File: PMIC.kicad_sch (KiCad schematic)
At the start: 57 parts, among them J10 Conn_01x03_Pin, J9 Conn_01x03_Pin, Q2 QM6015D, U7 MP2759AGQ-0000-Z, U8 MPM3620AGQV-P, U9 MPM3620AGQV-P

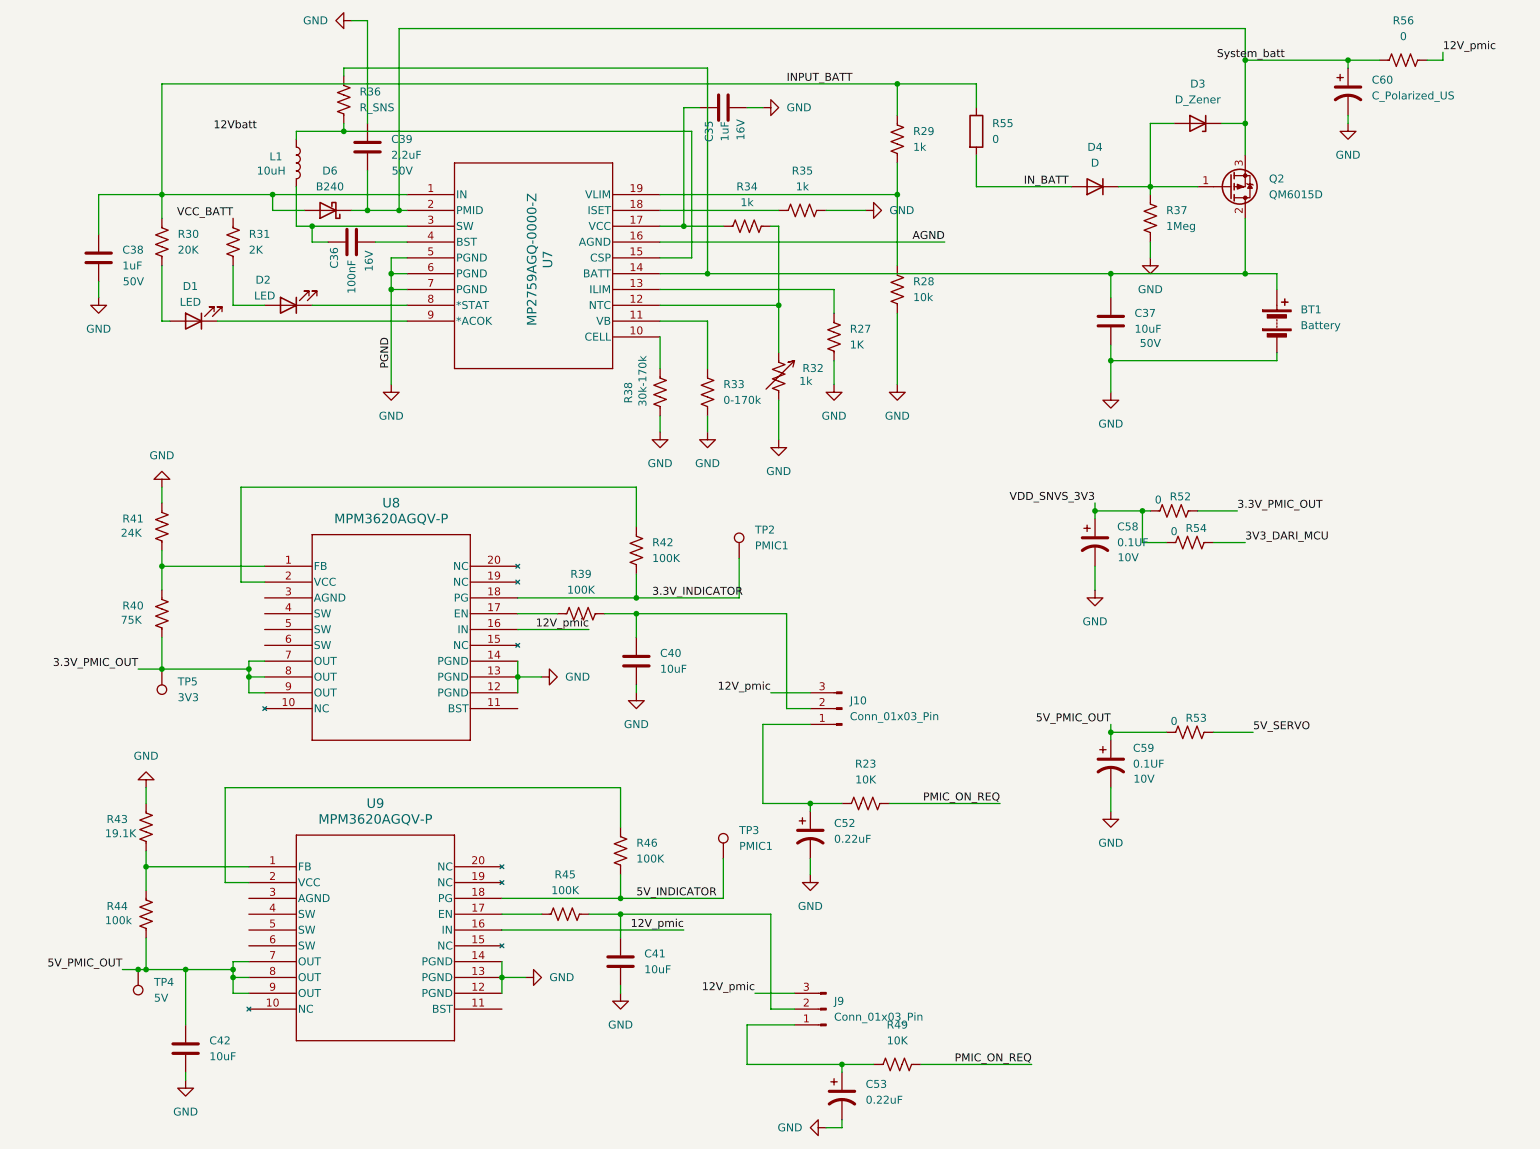
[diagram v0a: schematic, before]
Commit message: menambah lebih dari setengah footprint
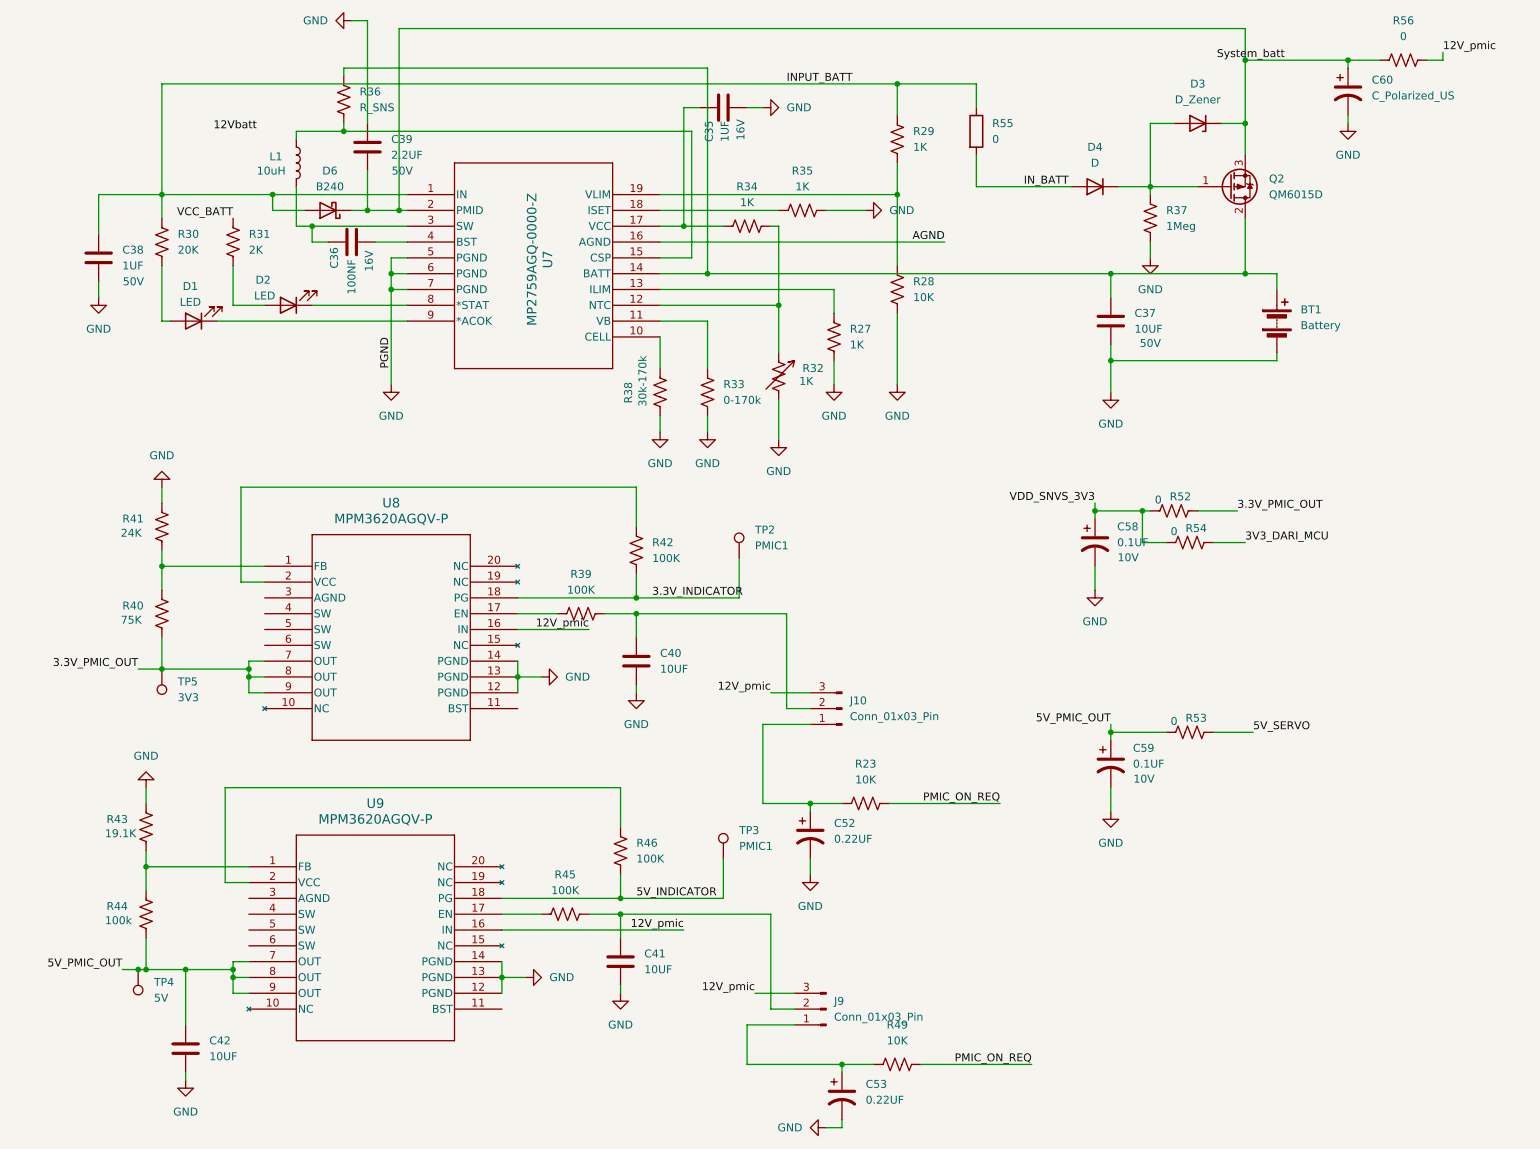
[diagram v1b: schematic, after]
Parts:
- C35, C38: value 1uF -> 1UF; footprint (none) -> Capacitor_SMD:C_0402_1005Metric
- C36: value 100nF -> 100NF; footprint (none) -> Capacitor_SMD:C_0402_1005Metric
- C37, C40, C41, C42: value 10uF -> 10UF; footprint (none) -> Capacitor_SMD:C_0603_1608Metric; MANUFACTURER (none) -> GRM188R61A106KE69D
- C39: value 2,2uF -> 2.2UF; footprint (none) -> Capacitor_SMD:C_0402_1005Metric
- C52, C53: value 0.22uF -> 0.22UF; footprint (none) -> Capacitor_SMD:C_0402_1005Metric; MANUFACTURER (none) -> CL10A226MQ8NRNE
- C58, C59: footprint (none) -> Capacitor_SMD:C_0402_1005Metric; MANUFACTURER (none) -> CC0402KRX5R6BB104
- R23, R27, R37, R39, R42, R44, R45, R46, R49, R52, R53, R54, R55, R56: footprint (none) -> Resistor_SMD:R_0402_1005Metric
- R28: value 10k -> 10K; footprint (none) -> Resistor_SMD:R_0402_1005Metric
- R29, R32, R34, R35: value 1k -> 1K; footprint (none) -> Resistor_SMD:R_0402_1005Metric
- U7: footprint QFN-19_MP2759A_MNP -> footprints:QFN-19_MP2759A_MNP
- U8, U9: footprint QFN3p0x5p0x1p6_MPM3606A_MNP -> footprints:QFN3p0x5p0x1p6_MPM3606A_MNP

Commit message: menambahkan beberapa component lagi
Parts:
- TP2, TP3, TP4, TP5: footprint (none) -> MountingHole:MountingHole_2.1mm
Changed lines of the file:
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@@
 			)
 		)
-		(property "Footprint" ""
+		(property "Footprint" "MountingHole:MountingHole_2.1mm"
 			(at 27.94 120.65 0)
 			(effects
@@
 			)
 		)
-		(property "Footprint" ""
+		(property "Footprint" "MountingHole:MountingHole_2.1mm"
 			(at 128.27 151.13 0)
 			(effects
@@
 			)
 		)
-		(property "Footprint" ""
+		(property "Footprint" "MountingHole:MountingHole_2.1mm"
 			(at 130.81 102.87 0)
 			(effects
@@
 			)
 		)
-		(property "Footprint" ""
+		(property "Footprint" "MountingHole:MountingHole_2.1mm"
 			(at 24.13 168.91 0)
 			(effects

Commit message: change the power bat system
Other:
- moved on the sheet: TP4
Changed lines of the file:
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@@
 	)
 	(junction
-		(at 29.21 168.91)
-		(diameter 0)
-		(color 0 0 0 0)
-	)
-	(junction
 		(at 207.01 33.02)
 		(diameter 0)
@@
 	)
 	(junction
+		(at 25.4 168.91)
+		(diameter 0)
+		(color 0 0 0 0)
+	)
+	(junction
 		(at 151.13 44.45)
 		(diameter 0)
@@
 	(wire
 		(pts
-			(xy 29.21 168.91) (xy 30.48 168.91)
-		)
-		(stroke
-			(width 0)
-			(type default)
-		)
-	)
-	(wire
-		(pts
 			(xy 57.15 52.07) (xy 57.15 49.53)
 		)
@@
 	(wire
 		(pts
-			(xy 26.67 168.91) (xy 29.21 168.91)
+			(xy 19.05 168.91) (xy 25.4 168.91)
 		)
 		(stroke
@@
 	(wire
 		(pts
+			(xy 25.4 168.91) (xy 30.48 168.91)
+		)
+		(stroke
+			(width 0)
+			(type default)
+		)
+	)
+	(wire
+		(pts
 			(xy 194.31 100.33) (xy 190.5 100.33)
 		)
@@
 	(global_label "12V_pmic"
 		(shape input)
-		(at 101.6 114.3 180)
+		(at 101.6 114.3 270)
 		(fields_autoplaced yes)
 		(effects
@@
 		)
 		(property "Intersheetrefs" "${INTERSHEET_REFS}"
-			(at 89.6039 114.3 0)
+			(at 101.6 126.2961 90)
 			(effects
 				(font
@@
 	(global_label "12V_pmic"
 		(shape input)
-		(at 116.84 162.56 180)
+		(at 116.84 162.56 0)
 		(fields_autoplaced yes)
 		(effects
@@
 				(size 1.27 1.27)
 			)
-			(justify right)
+			(justify left)
 		)
 		(property "Intersheetrefs" "${INTERSHEET_REFS}"
-			(at 104.8439 162.56 0)
+			(at 128.8361 162.56 0)
 			(effects
 				(font
 					(size 1.27 1.27)
 				)
-				(justify right)
+				(justify left)
 				(hide yes)
 			)
@@
 	(global_label "5V_PMIC_OUT"
 		(shape input)
-		(at 26.67 168.91 180)
+		(at 19.05 168.91 270)
 		(fields_autoplaced yes)
 		(effects
@@
 		)
 		(property "Intersheetrefs" "${INTERSHEET_REFS}"
-			(at 11.2267 168.91 0)
+			(at 19.05 184.3533 90)
 			(effects
 				(font
@@
 	(symbol
 		(lib_id "Connector:TestPoint")
-		(at 29.21 168.91 180)
+		(at 25.4 168.91 180)
 		(unit 1)
 		(exclude_from_sim no)
@@
 		(fields_autoplaced yes)
 		(property "Reference" "TP4"
-			(at 31.75 170.9419 0)
+			(at 27.94 170.9419 0)
 			(effects
 				(font
@@
 		)
 		(property "Value" "5V"
-			(at 31.75 173.4819 0)
+			(at 27.94 173.4819 0)
 			(effects
 				(font
@@
 		)
 		(property "Footprint" "MountingHole:MountingHole_2.1mm"
-			(at 24.13 168.91 0)
+			(at 20.32 168.91 0)
 			(effects
 				(font
@@
 		)
 		(property "Datasheet" "~"
-			(at 24.13 168.91 0)
+			(at 20.32 168.91 0)
 			(effects
 				(font
@@
 		)
 		(property "Description" "test point"
-			(at 29.21 168.91 0)
+			(at 25.4 168.91 0)
 			(effects
 				(font
@@
 		)
 		(property "DigikeyPartNumber" ""
-			(at 29.21 168.91 0)
+			(at 25.4 168.91 0)
 			(effects
 				(font
